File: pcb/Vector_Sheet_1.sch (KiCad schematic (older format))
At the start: 284 parts, among them J17 Main_Connector, J20 Edge_Connector_30_Pin, Q1 2N3904, Q4 2N3904, Q5 2N3904, Q6 2N3904, Q7 2N3904, Q8 2N3906

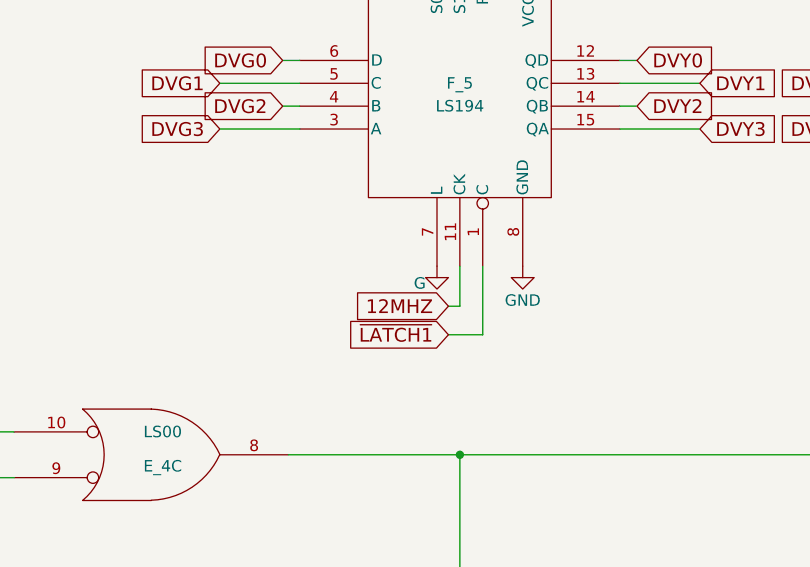
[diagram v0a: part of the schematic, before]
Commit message: Fixed errors on the schematic
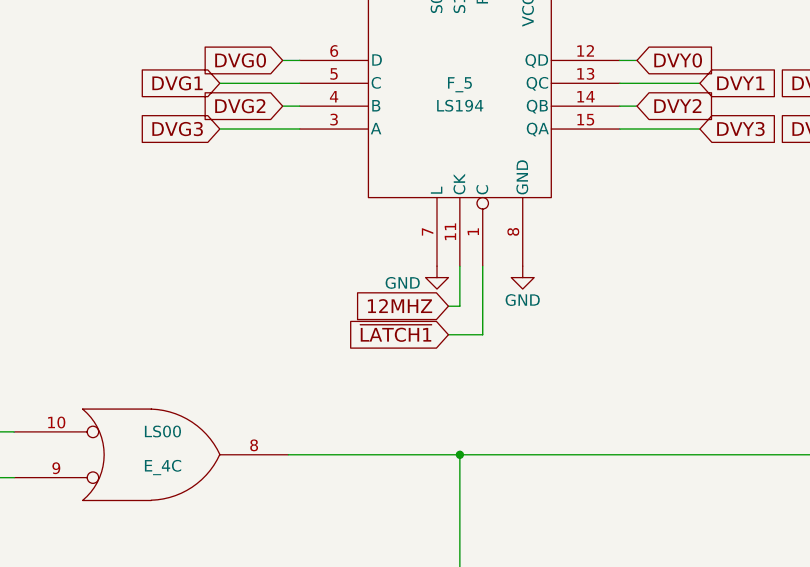
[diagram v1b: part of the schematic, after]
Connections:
- net GND: now also F_5.7 (L)
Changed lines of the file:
@@
 Text GLabel 38300 3075 1    60   Input ~ 0
 P2
-$Comp
-L Star_Wars_Vector_PCB:G #PWR03
-U 1 1 5CEC2702
-P 38100 4575
-F 0 "#PWR03" H 38100 4325 50  0001 C CNN
-F 1 "G" H 38025 4500 50  0000 C CNN
-F 2 "" H 38100 4575 50  0001 C CNN
-F 3 "" H 38100 4575 50  0001 C CNN
-	1    38100 4575
-	1    0    0    -1
-$EndComp
 Text GLabel 38150 4875 0    60   Input ~ 0
 ~LATCH1
@@
 Wire Wire Line
 	5000 21525 4750 21525
+$Comp
+L power:GND #PWR?
+U 1 1 60B7F56D
+P 38100 4575
+F 0 "#PWR?" H 38100 4325 50  0001 C CNN
+F 1 "GND" H 37950 4500 50  0000 C CNN
+F 2 "" H 38100 4575 50  0001 C CNN
+F 3 "" H 38100 4575 50  0001 C CNN
+	1    38100 4575
+	1    0    0    -1
+$EndComp
 $EndSCHEMATC
